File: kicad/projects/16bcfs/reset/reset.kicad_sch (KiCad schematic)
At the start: 26 parts, among them J1 Conn_01x16_Pin, U1 74HC00, U2 74HC08, U3 74HC32, U4 74HC00, U5 74HC74, U6 74HC00, U7 74HC02, U8 74HC123, U9 74HC03

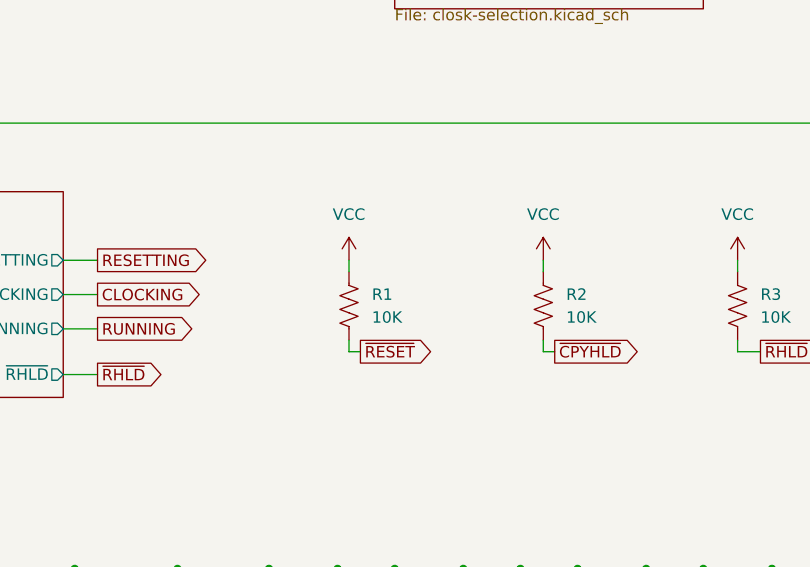
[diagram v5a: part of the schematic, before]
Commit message: Clean up the Reset and Clock Modules
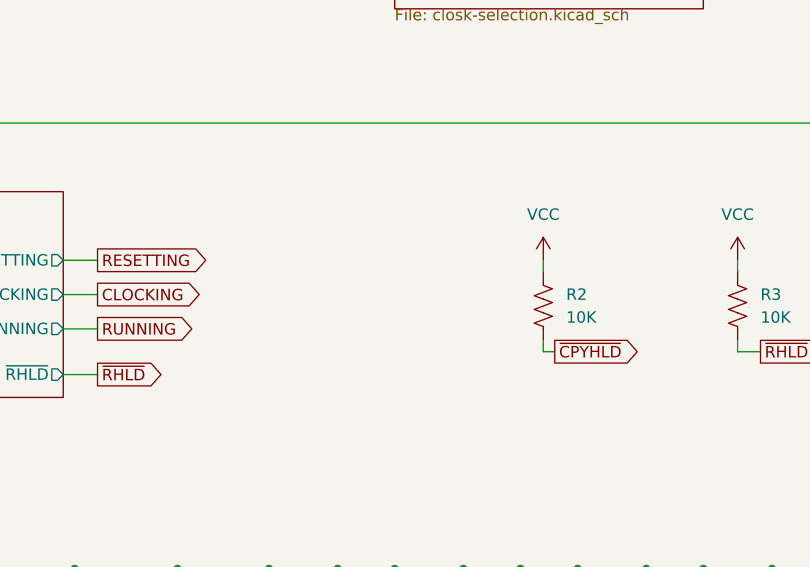
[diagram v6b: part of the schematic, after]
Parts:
- removed R1: 10K, symbol Device:R_US
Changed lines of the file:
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@@
-    (stroke (width 0) (type default))
-  )
-  (wire (pts (xy 130.81 76.2) (xy 130.81 77.47))
     (stroke (width 0) (type default))
   )
@@
     (stroke (width 0) (type default))
   )
-  (wire (pts (xy 130.81 86.36) (xy 132.08 86.36))
-    (stroke (width 0) (type default))
-  )
   (wire (pts (xy 88.9 135.89) (xy 100.33 135.89))
     (stroke (width 0) (type default))
@@
   )
   (wire (pts (xy 189.23 162.56) (xy 189.23 165.1))
-    (stroke (width 0) (type default))
-  )
-  (wire (pts (xy 130.81 85.09) (xy 130.81 86.36))
     (stroke (width 0) (type default))
   )
@@
     (property "Intersheetrefs" "${INTERSHEET_REFS}" (at 122.9262 39.37 0)
       (effects (font (size 1.27 1.27)) (justify right) hide)
-    )
-  )
-  (global_label "~{RESET}" (shape output) (at 132.08 86.36 0) (fields_autoplaced)
-    (effects (font (size 1.27 1.27)) (justify left))
-    (property "Intersheetrefs" "${INTERSHEET_REFS}" (at 140.8103 86.36 0)
-      (effects (font (size 1.27 1.27)) (justify left) hide)
     )
   )
@@
         (path "/d0ae44e5-d74e-4df6-bf3d-e0535c5a7785"
           (reference "#PWR03") (unit 1)
-        )
-      )
-    )
-  )
-  (symbol (lib_id "Device:R_US") (at 130.81 81.28 0) (unit 1)
-    (in_bom yes) (on_board yes) (dnp no) (fields_autoplaced)
-    (property "Reference" "R1" (at 133.35 80.01 0)
-      (effects (font (size 1.27 1.27)) (justify left))
-    )
-    (property "Value" "10K" (at 133.35 82.55 0)
-      (effects (font (size 1.27 1.27)) (justify left))
-    )
-    (property "Footprint" "" (at 131.826 81.534 90)
-      (effects (font (size 1.27 1.27)) hide)
-    )
-    (property "Datasheet" "~" (at 130.81 81.28 0)
-      (effects (font (size 1.27 1.27)) hide)
-    )
-    (pin "2")
-    (pin "1")
-    (instances
-      (project "reset"
-        (path "/d0ae44e5-d74e-4df6-bf3d-e0535c5a7785"
-          (reference "R1") (unit 1)
         )
       )
@@
         )
       )
-    )
-  )
-  (symbol (lib_id "power:VCC") (at 130.81 76.2 0) (mirror y) (unit 1)
-    (in_bom yes) (on_board yes) (dnp no)
-    (property "Reference" "#PWR01" (at 130.81 80.01 0)
-      (effects (font (size 1.27 1.27)) hide)
-    )
-    (property "Value" "VCC" (at 130.81 71.12 0)
-      (effects (font (size 1.27 1.27)))
-    )
-    (property "Footprint" "" (at 130.81 76.2 0)
-      (effects (font (size 1.27 1.27)) hide)
-    )
-    (property "Datasheet" "" (at 130.81 76.2 0)
-      (effects (font (size 1.27 1.27)) hide)
-    )
-    (pin "1")
-    (instances
-      (project "reset"
-        (path "/d0ae44e5-d74e-4df6-bf3d-e0535c5a7785"
-          (reference "#PWR01") (unit 1)
-        )
-      )

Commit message: Some KiCad Cleanup
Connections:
- net SYS_CLK renamed CLK
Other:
- sheet Clock Selection & Timing ports: added CLK; removed SYS_CLK
- note added: "Rest of the Sys"
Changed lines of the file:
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@@
     (effects (font (size 1.27 1.27)) (justify left top))
+  )
+  (text "Rest of \nthe Sys" (at 259.08 111.76 0)
+    (effects (font (size 1.27 1.27)) (justify left bottom) (href "#1"))
   )
   (global_label "RUNNING" (shape input) (at 27.94 161.29 180) (fields_autoplaced)
@@
     )
   )
-  (global_label "SYS_CLK" (shape output) (at 172.72 33.02 0) (fields_autoplaced)
+  (global_label "CLK" (shape output) (at 172.72 33.02 0) (fields_autoplaced)
     (effects (font (size 1.27 1.27)) (justify left))
-    (property "Intersheetrefs" "${INTERSHEET_REFS}" (at 183.7485 33.02 0)
+    (property "Intersheetrefs" "${INTERSHEET_REFS}" (at 179.2733 33.02 0)
       (effects (font (size 1.27 1.27)) (justify left) hide)
     )
@@
     )
   )
-  (global_label "SYS_CLK" (shape input) (at 252.73 109.22 180) (fields_autoplaced)
-    (effects (font (size 1.27 1.27)) (justify right))
-    (property "Intersheetrefs" "${INTERSHEET_REFS}" (at 241.7015 109.22 0)
+  (global_label "CLK" (shape input) (at 252.73 109.22 180) (fields_autoplaced)
+    (effects (font (size 1.27 1.27)) (justify right))
+    (property "Intersheetrefs" "${INTERSHEET_REFS}" (at 246.1767 109.22 0)
       (effects (font (size 1.27 1.27)) (justify right) hide)
     )
@@
       (effects (font (size 1.27 1.27)) (justify left))
     )
-    (pin "SYS_CLK" output (at 170.18 33.02 0)
+    (pin "CLK" output (at 170.18 33.02 0)
       (effects (font (size 1.27 1.27)) (justify right))
     )
